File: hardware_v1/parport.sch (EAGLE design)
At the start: 13 parts, among them IC1 74LS541DW, IC2 74LS541DW, IC3 74LS541DW, K1 PIN20X2

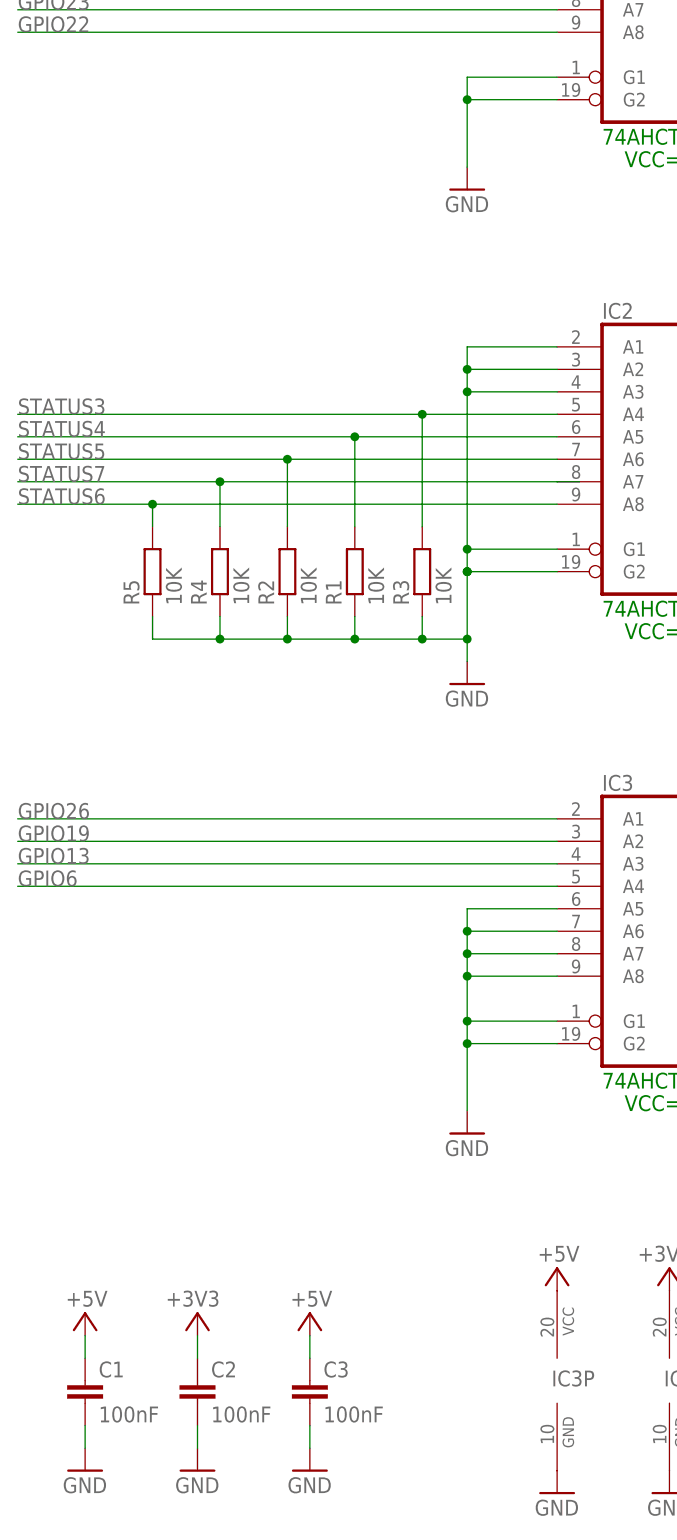
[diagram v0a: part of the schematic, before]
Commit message: hardware_v1: status 10k pd -> 4.3k pu
Change the 10K pulldowns to 4.3K pullups.
4.7K is what would normally be used here but I had some
803 4.3K's on hand.

Place some vias for the pullups and also for the unrouted
CONTROL3 line.  Before we had a one sided board which is
a bit easier to fab with the CNC.  Place vias so it can
still be made one sided without requiring connectors to
have plated through holes.  A small number of jumper wires
will need to be soldered to vias on aone sided board.
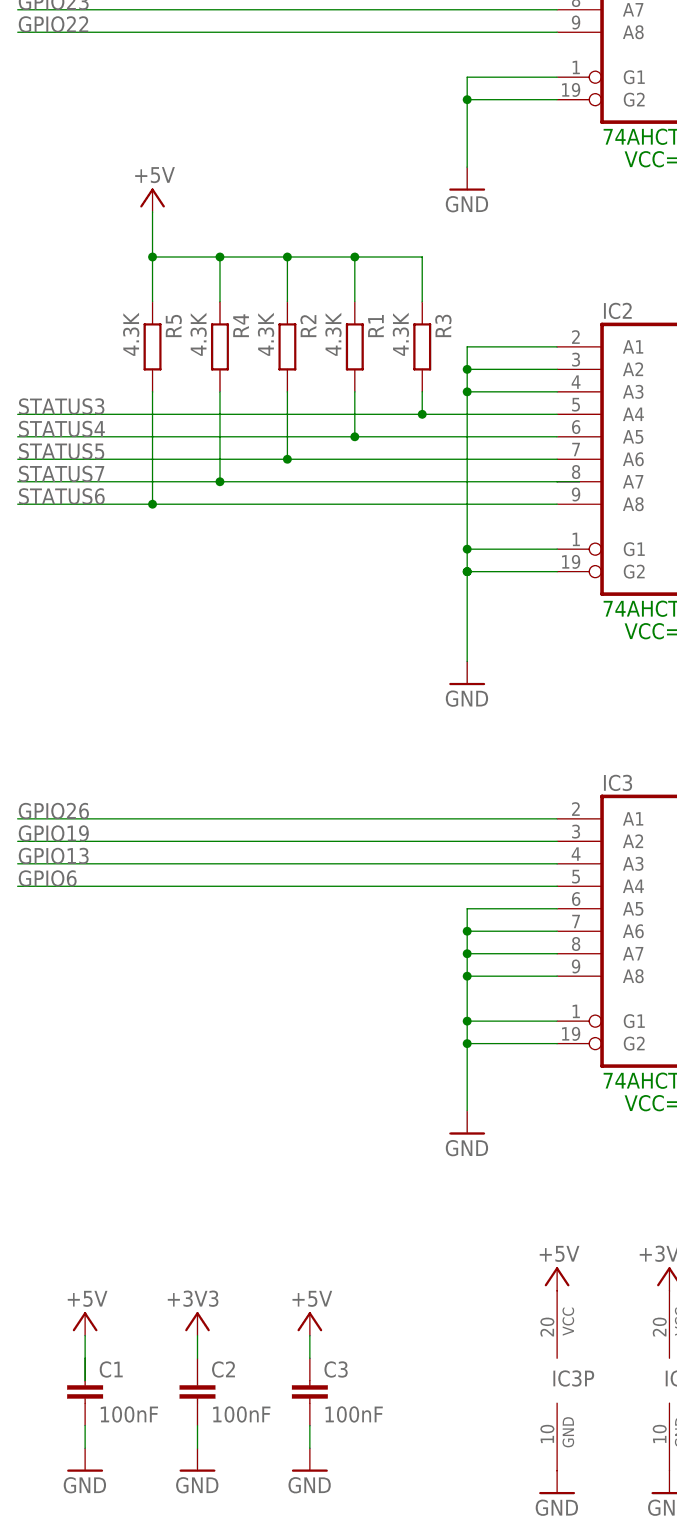
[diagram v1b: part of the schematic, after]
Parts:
- R1, R2, R3, R4, R5: value 10K -> 4.3K
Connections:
- net +5V: now also R1.1, R2.1, R3.1, R4.1, R5.1
- net GND: no longer R1.1, R2.1, R3.1, R4.1, R5.1
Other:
- moved on the sheet: R1, R2, R3, R4, R5
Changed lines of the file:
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@@
 <part name="GND4" library="supply1" deviceset="GND" device=""/>
 <part name="GND5" library="supply1" deviceset="GND" device=""/>
-<part name="R1" library="resistor" deviceset="R-EU_" device="R0805" value="10K"/>
-<part name="R2" library="resistor" deviceset="R-EU_" device="R0805" value="10K"/>
-<part name="R3" library="resistor" deviceset="R-EU_" device="R0805" value="10K"/>
-<part name="R4" library="resistor" deviceset="R-EU_" device="R0805" value="10K"/>
-<part name="R5" library="resistor" deviceset="R-EU_" device="R0805" value="10K"/>
+<part name="R1" library="resistor" deviceset="R-EU_" device="R0805" value="4.3K"/>
+<part name="R2" library="resistor" deviceset="R-EU_" device="R0805" value="4.3K"/>
+<part name="R3" library="resistor" deviceset="R-EU_" device="R0805" value="4.3K"/>
+<part name="R4" library="resistor" deviceset="R-EU_" device="R0805" value="4.3K"/>
+<part name="R5" library="resistor" deviceset="R-EU_" device="R0805" value="4.3K"/>
 <part name="C1" library="resistor" deviceset="C-EU" device="C0805" value="100nF"/>
 <part name="GND6" library="supply1" deviceset="GND" device=""/>
@@
 <part name="GND12" library="supply1" deviceset="GND" device=""/>
 <part name="+3V3" library="supply1" deviceset="+3V3" device=""/>
+<part name="P+6" library="supply1" deviceset="+5V" device=""/>
 </parts>
 <sheets>
@@
 <instance part="GND4" gate="1" x="104.14" y="121.92"/>
 <instance part="GND5" gate="1" x="104.14" y="71.12"/>
-<instance part="R1" gate="G$1" x="91.44" y="134.62" rot="R90"/>
-<instance part="R2" gate="G$1" x="83.82" y="134.62" rot="R90"/>
-<instance part="R3" gate="G$1" x="99.06" y="134.62" rot="R90"/>
-<instance part="R4" gate="G$1" x="76.2" y="134.62" rot="R90"/>
-<instance part="R5" gate="G$1" x="68.58" y="134.62" rot="R90"/>
+<instance part="R1" gate="G$1" x="91.44" y="160.02" rot="R270"/>
+<instance part="R2" gate="G$1" x="83.82" y="160.02" rot="R270"/>
+<instance part="R3" gate="G$1" x="99.06" y="160.02" rot="R270"/>
+<instance part="R4" gate="G$1" x="76.2" y="160.02" rot="R270"/>
+<instance part="R5" gate="G$1" x="68.58" y="160.02" rot="R270"/>
 <instance part="C1" gate="G$1" x="60.96" y="43.18"/>
 <instance part="GND6" gate="1" x="60.96" y="33.02"/>
@@
 <instance part="+3V3" gate="G$1" x="127" y="55.88" smashed="yes">
 <attribute name="VALUE" x="129.54" y="58.42" size="1.778" layer="96" rot="R180"/>
+</instance>
+<instance part="P+6" gate="1" x="68.58" y="177.8" smashed="yes">
+<attribute name="VALUE" x="71.12" y="180.34" size="1.778" layer="96" rot="R180"/>
 </instance>
 </instances>
@@
 <pinref part="GND4" gate="1" pin="GND"/>
 <pinref part="IC2" gate="A" pin="G2"/>
-<wire x1="104.14" y1="134.62" x2="104.14" y2="127" width="0.1524" layer="91"/>
-<wire x1="104.14" y1="127" x2="104.14" y2="124.46" width="0.1524" layer="91"/>
+<wire x1="104.14" y1="134.62" x2="104.14" y2="124.46" width="0.1524" layer="91"/>
 <wire x1="114.3" y1="134.62" x2="104.14" y2="134.62" width="0.1524" layer="91"/>
 <junction x="104.14" y="134.62"/>
@@
 <wire x1="114.3" y1="137.16" x2="104.14" y2="137.16" width="0.1524" layer="91"/>
 <junction x="104.14" y="137.16"/>
-<pinref part="R5" gate="G$1" pin="1"/>
-<wire x1="68.58" y1="129.54" x2="68.58" y2="127" width="0.1524" layer="91"/>
-<wire x1="68.58" y1="127" x2="76.2" y2="127" width="0.1524" layer="91"/>
-<junction x="104.14" y="127"/>
-<pinref part="R4" gate="G$1" pin="1"/>
-<wire x1="76.2" y1="127" x2="83.82" y2="127" width="0.1524" layer="91"/>
-<wire x1="83.82" y1="127" x2="91.44" y2="127" width="0.1524" layer="91"/>
-<wire x1="91.44" y1="127" x2="99.06" y2="127" width="0.1524" layer="91"/>
-<wire x1="99.06" y1="127" x2="104.14" y2="127" width="0.1524" layer="91"/>
-<wire x1="76.2" y1="129.54" x2="76.2" y2="127" width="0.1524" layer="91"/>
-<junction x="76.2" y="127"/>
-<pinref part="R2" gate="G$1" pin="1"/>
-<wire x1="83.82" y1="129.54" x2="83.82" y2="127" width="0.1524" layer="91"/>
-<junction x="83.82" y="127"/>
-<pinref part="R1" gate="G$1" pin="1"/>
-<wire x1="91.44" y1="129.54" x2="91.44" y2="127" width="0.1524" layer="91"/>
-<junction x="91.44" y="127"/>
-<pinref part="R3" gate="G$1" pin="1"/>
-<wire x1="99.06" y1="129.54" x2="99.06" y2="127" width="0.1524" layer="91"/>
-<junction x="99.06" y="127"/>
 </segment>
 <segment>
@@
 <pinref part="C1" gate="G$1" pin="1"/>
 <wire x1="60.96" y1="48.26" x2="60.96" y2="45.72" width="0.1524" layer="91"/>
+<wire x1="60.96" y1="45.72" x2="60.96" y2="43.18" width="0.1524" layer="91"/>
 </segment>
 <segment>
@@
 <pinref part="IC1" gate="P" pin="VCC"/>
 <pinref part="P+5" gate="1" pin="+5V"/>
+</segment>
+<segment>
+<pinref part="R3" gate="G$1" pin="1"/>
+<wire x1="99.06" y1="165.1" x2="99.06" y2="170.18" width="0.1524" layer="91"/>
+<wire x1="99.06" y1="170.18" x2="91.44" y2="170.18" width="0.1524" layer="91"/>
+<wire x1="91.44" y1="170.18" x2="83.82" y2="170.18" width="0.1524" layer="91"/>
+<wire x1="83.82" y1="170.18" x2="76.2" y2="170.18" width="0.1524" layer="91"/>
+<wire x1="76.2" y1="170.18" x2="68.58" y2="170.18" width="0.1524" layer="91"/>
+<pinref part="R4" gate="G$1" pin="1"/>
+<wire x1="76.2" y1="165.1" x2="76.2" y2="170.18" width="0.1524" layer="91"/>
+<junction x="76.2" y="170.18"/>
+<pinref part="R2" gate="G$1" pin="1"/>
+<wire x1="83.82" y1="165.1" x2="83.82" y2="170.18" width="0.1524" layer="91"/>
+<junction x="83.82" y="170.18"/>
+<pinref part="R1" gate="G$1" pin="1"/>
+<wire x1="91.44" y1="165.1" x2="91.44" y2="170.18" width="0.1524" layer="91"/>
+<junction x="91.44" y="170.18"/>
+<pinref part="P+6" gate="1" pin="+5V"/>
+<wire x1="68.58" y1="175.26" x2="68.58" y2="170.18" width="0.1524" layer="91"/>
+<pinref part="R5" gate="G$1" pin="1"/>
+<wire x1="68.58" y1="165.1" x2="68.58" y2="170.18" width="0.1524" layer="91"/>
+<junction x="68.58" y="170.18"/>
 </segment>
 </net>
@@
 <junction x="68.58" y="142.24"/>
 <pinref part="R5" gate="G$1" pin="2"/>
-<wire x1="68.58" y1="139.7" x2="68.58" y2="142.24" width="0.1524" layer="91"/>
+<wire x1="68.58" y1="154.94" x2="68.58" y2="142.24" width="0.1524" layer="91"/>
 </segment>
 </net>
@@
 <junction x="83.82" y="147.32"/>
 <pinref part="R2" gate="G$1" pin="2"/>
-<wire x1="83.82" y1="139.7" x2="83.82" y2="147.32" width="0.1524" layer="91"/>
+<wire x1="83.82" y1="154.94" x2="83.82" y2="147.32" width="0.1524" layer="91"/>
 </segment>
 </net>
@@
 <junction x="99.06" y="152.4"/>
 <pinref part="R3" gate="G$1" pin="2"/>
-<wire x1="99.06" y1="139.7" x2="99.06" y2="152.4" width="0.1524" layer="91"/>
+<wire x1="99.06" y1="154.94" x2="99.06" y2="152.4" width="0.1524" layer="91"/>
 </segment>
 </net>
@@
 <junction x="91.44" y="149.86"/>
 <pinref part="R1" gate="G$1" pin="2"/>
-<wire x1="91.44" y1="139.7" x2="91.44" y2="149.86" width="0.1524" layer="91"/>
+<wire x1="91.44" y1="154.94" x2="91.44" y2="149.86" width="0.1524" layer="91"/>
 </segment>
 </net>
@@
 <junction x="76.2" y="144.78"/>
 <pinref part="R4" gate="G$1" pin="2"/>
-<wire x1="76.2" y1="139.7" x2="76.2" y2="144.78" width="0.1524" layer="91"/>
-</segment>
-</net>
+<wire x1="76.2" y1="154.94" x2="76.2" y2="144.78" width="0.1524" layer="91"/>
+</segment>
+</net>
